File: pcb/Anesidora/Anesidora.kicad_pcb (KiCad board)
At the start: 2 copper layers, 305 x 123.5 mm, 198 parts, among them J1 Conn_01x06_Socket, SW1 SW_Push_45deg, SW10 SW_Push_45deg, SW11 SW_Push_45deg, SW12 SW_Push_45deg, SW13 SW_Push_45deg, SW14 SW_Push_45deg, SW15 SW_Push_45deg, SW16 SW_Push_45deg, SW17 SW_Push_45deg, SW18 SW_Push_45deg, SW19 SW_Push_45deg, SW2 SW_Push_45deg, SW20 SW_Push_45deg, SW21 SW_Push_45deg, SW22 SW_Push_45deg, SW23 SW_Push_45deg, SW24 SW_Push_45deg, SW25 SW_Push_45deg, SW26 SW_Push_45deg, SW27 SW_Push_45deg, SW28 SW_Push_45deg, SW29 SW_Push_45deg, SW3 SW_Push_45deg, SW30 SW_Push_45deg, SW31 SW_Push_45deg, SW32 SW_Push_45deg, SW33 SW_Push_45deg, SW34 SW_Push_45deg, SW35 SW_Push_45deg, SW36 SW_Push_45deg, SW37 SW_Push_45deg, SW38 SW_Push_45deg, SW39 SW_Push_45deg, SW4 SW_Push_45deg, SW40 SW_Push_45deg, SW41 SW_Push_45deg, SW42 SW_Push_45deg, SW43 SW_Push_45deg, SW44 SW_Push_45deg, SW45 SW_Push_45deg, SW46 SW_Push_45deg, SW47 SW_Push_45deg, SW48 RotaryEncoder_Switch, SW49 SW_Push_45deg, SW5 SW_Push_45deg, SW50 SW_Push_45deg, SW51 SW_Push_45deg, SW52 SW_Push_45deg, SW53 SW_Push_45deg, SW54 SW_Push_45deg, SW55 SW_Push_45deg, SW56 SW_Push_45deg, SW57 SW_Push_45deg, SW58 SW_Push_45deg, SW59 SW_Push_45deg, SW6 SW_Push_45deg, SW60 SW_Push_45deg, SW61 SW_Push_45deg, SW62 SW_Push_45deg, SW63 SW_Push_45deg, SW64 SW_Push_45deg, SW65 SW_Push_45deg, SW66 SW_Push_45deg, SW67 SW_Push_45deg, SW68 SW_Push_45deg, SW69 SW_Push_45deg, SW7 SW_Push_45deg, SW8 SW_Push_45deg, SW9 SW_Push_45deg, U1 Pico

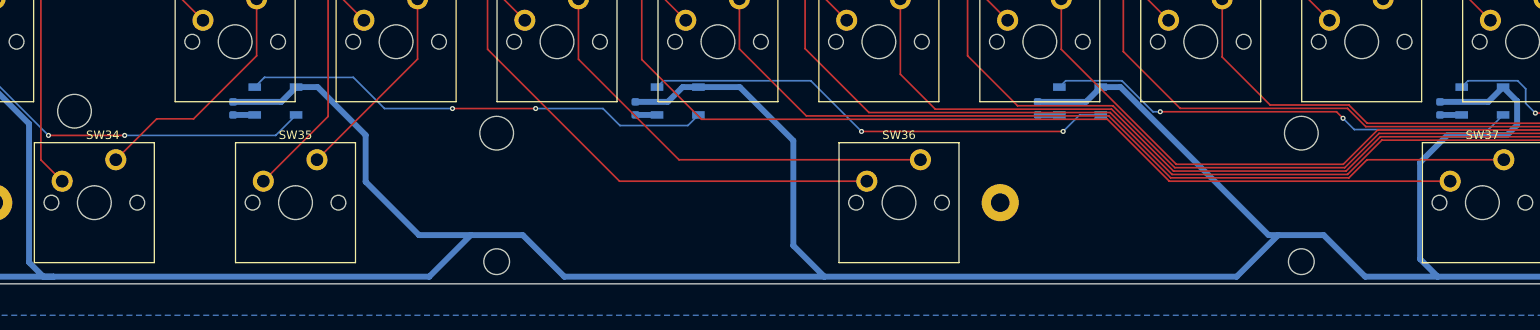
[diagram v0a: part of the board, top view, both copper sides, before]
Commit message: fix spacebar size
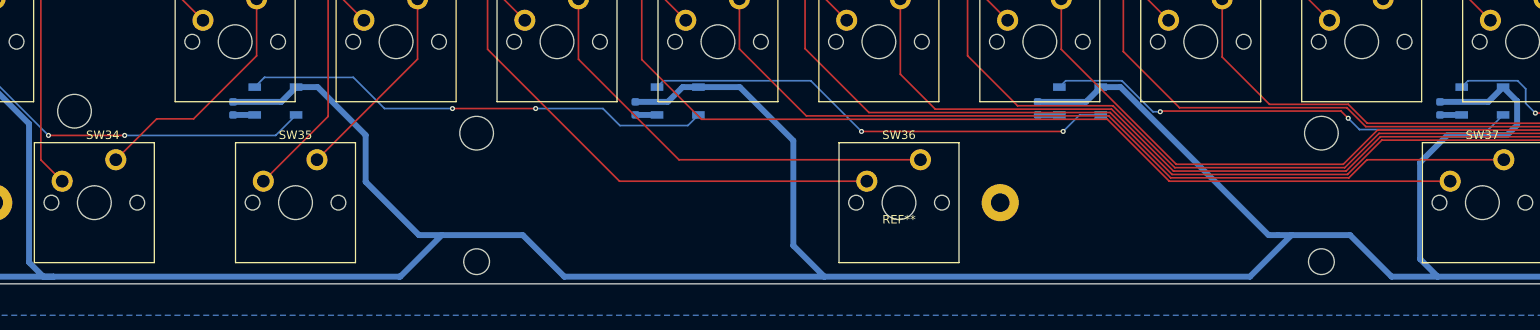
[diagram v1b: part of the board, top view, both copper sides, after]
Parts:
- removed the REF** at (237.0, 202.0)
- added REF**: Stabilizer_Cherry_MX_6.25u, PCM_Mounting_Keyboard_Stabilizer:Stabilizer_Cherry_MX_6.25u, F.Cu at (237.0, 202.0)
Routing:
- net +5V: track 1191.0 -> 1189.1 mm

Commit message: add mounting holes
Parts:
- added H11: MountingHole, MountingHole:MountingHole_2.2mm_M2_Pad, F.Cu at (182.2, 134.8)
- added H12: MountingHole, MountingHole:MountingHole_2.2mm_M2_Pad, F.Cu at (334.6, 134.8)
- added H13: MountingHole, MountingHole:MountingHole_2.2mm_M2_Pad, F.Cu at (344.2, 189.5)
- added H14: MountingHole, MountingHole:MountingHole_2.2mm_M2_Pad, F.Cu at (390.1, 159.2)
- added H15: MountingHole, MountingHole:MountingHole_2.2mm_M2_Pad, F.Cu at (234.6, 172.9)
- added H16: MountingHole, MountingHole:MountingHole_2.2mm_M2_Pad, F.Cu at (310.8, 172.9)
- moved H6 193.3 mm to (158.4, 172.9)
- moved H10 48.6 mm to (198.0, 202.0)
- moved H7 19.1 mm to (391.1, 125.8)
- moved H9 15.0 mm to (264.0, 202.0)
- renumbered U1 to Pico, SW_RESET1 to RESET
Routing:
- net Net-(D40-A): track 204.5 -> 215.0 mm
- net Col 8: track 441.3 -> 449.7 mm
- net Col 2: track 345.1 -> 349.9 mm
- net Col 4: track 407.2 -> 411.7 mm
- net Net-(D81-DOUT): track 56.0 -> 60.4 mm
- net Net-(D37-A): track 226.1 -> 229.4 mm
- net Net-(D38-A): track 220.5 -> 223.7 mm
- net Net-(D39-A): track 214.4 -> 217.5 mm
- net Col 6: track 434.5 -> 437.5 mm
- net Net-(D36-A): track 180.5 -> 182.7 mm
- net Col 5: track 495.8 -> 497.8 mm
- net Net-(D61-A): track 104.5 -> 103.0 mm
- net Net-(D63-A): track 96.8 -> 98.3 mm
- net Net-(D49-A): track 49.1 -> 50.5 mm
- net Net-(D56-A): track 71.2 -> 72.6 mm
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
